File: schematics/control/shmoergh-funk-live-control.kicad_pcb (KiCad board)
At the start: 2 copper layers, 225 x 102.5 mm, 162 parts, among them J1 Power, J2 Power, J3 Power, J4 Power, J5 Power, J6 Power, Q1 BC548C, Q2 BC558, Q3 BC548, Q4 BC548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

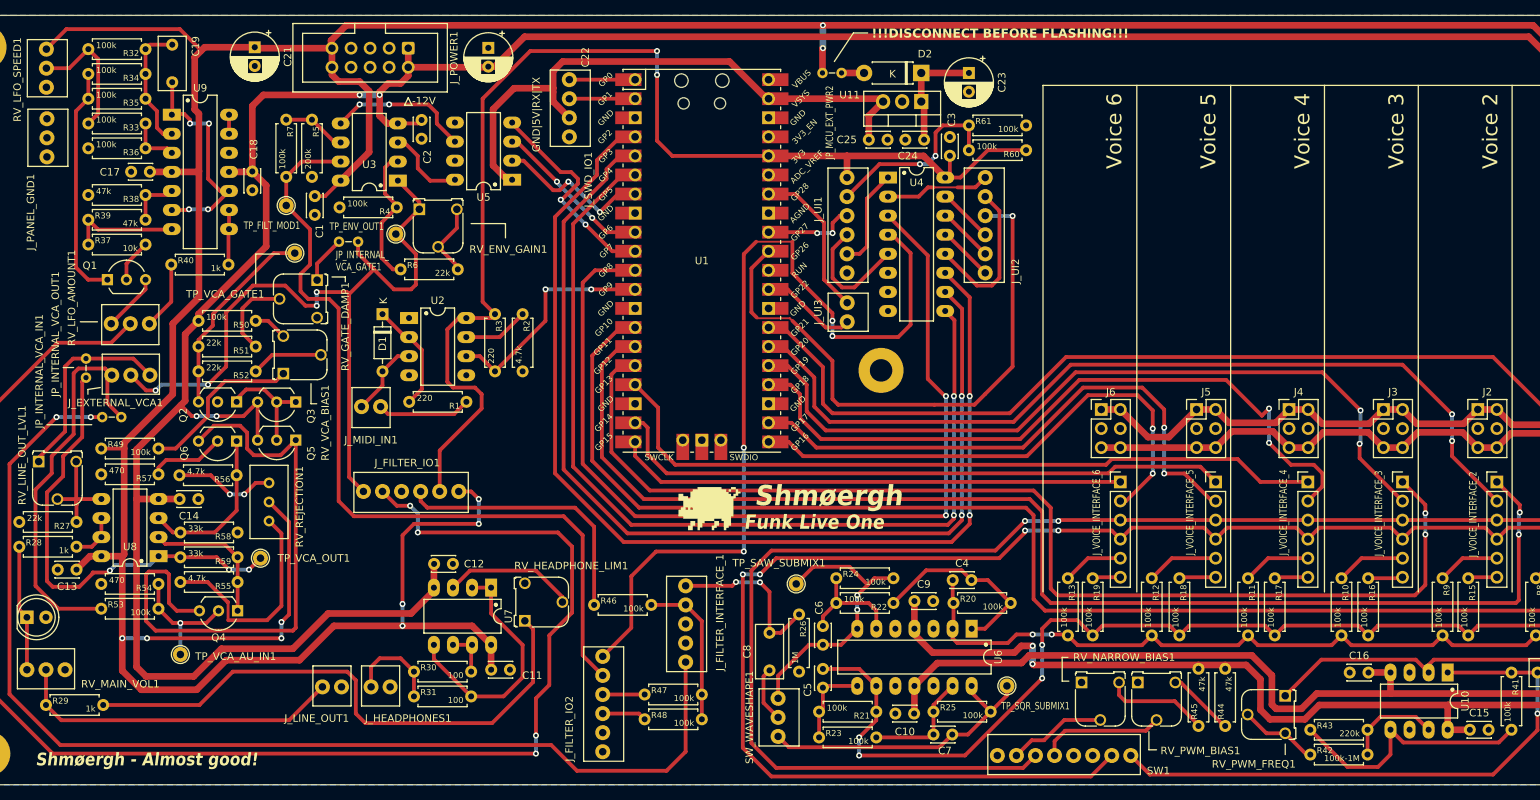
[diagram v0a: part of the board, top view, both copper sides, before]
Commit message: Simplified PWM switch IO
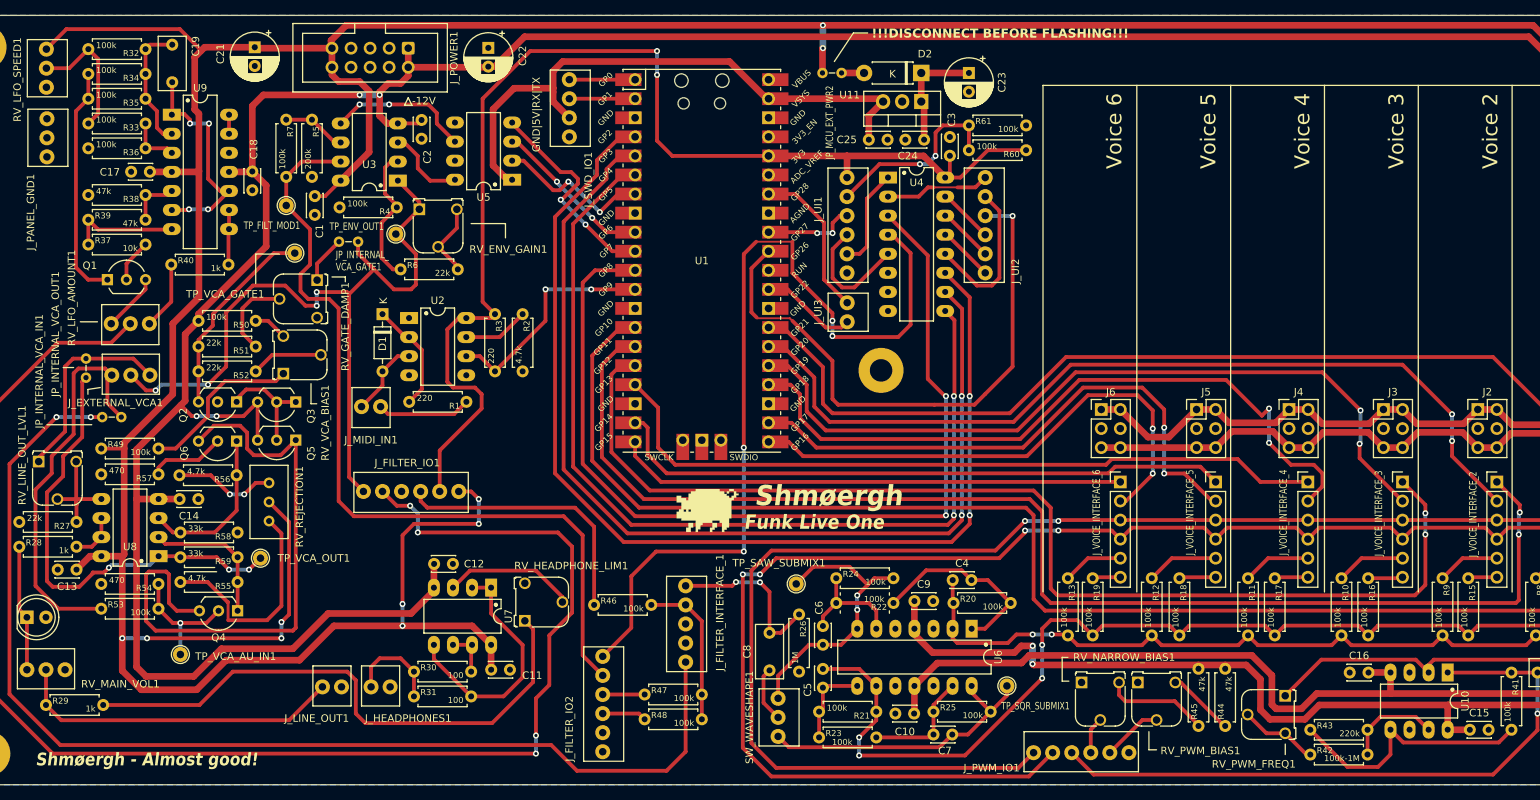
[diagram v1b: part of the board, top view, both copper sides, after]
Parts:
- removed SW1: SW_DP3T, Shmoergh_Custom_Footprints:NSL25_01x08_Vertical
- added J_PWM_IO1: Conn_01x06, Shmoergh_Custom_Footprints:NSL25_01x06_Vertical, F.Cu at (181.5, 133.2)
- moved G*** 0.36 mm to (138.0, 101.0)
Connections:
- net Net-(C20-Pad2) renamed PWM_LFO
- RV_NARROW_BIAS1 pad 2: Net-(RV_NARROW_BIAS1-Pad2) -> PWM_NARROW_BIAS
- RV_PWM_BIAS1 pad 2: Net-(RV_PWM_BIAS1-Pad2) -> PWM_LFO_BIAS
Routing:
- net Net-(RV_PWM_BIAS1-Pad2): track 16.7 -> 0.00 mm
- net Net-(RV_NARROW_BIAS1-Pad2): track 13.1 -> 0.00 mm
- net PWM_LFO: track 77.3 -> 85.4 mm
- net PWM_LFO_BIAS: track 0.00 -> 8.03 mm
- net /LFO + PWM/PWM_OUT: track 197.4 -> 189.7 mm
- net PWM_NARROW_BIAS: track 0.00 -> 4.88 mm

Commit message: Updated schem. + added JLCPCB gerbers
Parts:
- moved H1 17.5 mm to (275.8, 39.1)
- moved H2 17.5 mm to (275.8, 133.5)
- moved J_VOICE_INTERFACE_1 17.4 mm to (273.1, 97.2)
- moved J1 17.4 mm to (270.6, 87.5)
- moved R14 17.4 mm to (269.2, 110.0)
- moved R8 17.4 mm to (265.8, 110.0)
- moved J2 14.5 mm to (255.1, 87.5)
- moved J_VOICE_INTERFACE_2 14.5 mm to (257.7, 97.2)
- moved R15 14.5 mm to (253.9, 110.0)
- moved R9 14.5 mm to (250.4, 110.0)
- moved J3 11.7 mm to (239.8, 87.5)
- moved J_VOICE_INTERFACE_3 11.7 mm to (242.3, 97.2)
- moved R10 11.7 mm to (234.2, 110.0)
- moved R16 11.7 mm to (237.7, 110.0)
- moved J4 8.76 mm to (224.3, 87.5)
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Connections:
- U1 pad 4: MUX_A -> MUX_C
- U1 pad 6: MUX_C -> MUX_A
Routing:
- net +12V: track 760.3 -> 816.0 mm, vias 14 -> 12
- net -12V: track 624.5 -> 673.6 mm, vias 4 -> 6
- net MUX_A: track 145.2 -> 107.0 mm, vias 2 -> 6
- net MUX_BINARY: track 126.3 -> 159.9 mm, vias 2 -> 6
- net MUX_B: track 135.5 -> 108.8 mm, vias 2 -> 6
- net Net-(U6C--): track 129.5 -> 152.2 mm
- net /LFO + PWM/PWM_OUT: track 189.7 -> 208.0 mm, vias 4 -> 2
- net /LFO + PWM/PULSE_WIDTH: track 177.5 -> 195.0 mm, vias 2 -> 0
- net /Digital/AMP_1: track 131.8 -> 149.2 mm
- net Net-(U6A--): track 91.8 -> 109.1 mm
- net /Digital/RESET_1: track 189.0 -> 203.9 mm, vias 0 -> 2
- net /Digital/AMP_2: track 117.4 -> 131.9 mm
- net MUX_C: track 125.7 -> 112.8 mm, vias 2 -> 6
- net /Digital/RESET_2: track 171.6 -> 184.5 mm, vias 2 -> 4
- net /Digital/Digital UI/RING_TIME: track 77.8 -> 89.4 mm
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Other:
- board size 225 x 102.5 mm -> 242.5 x 102.5 mm
